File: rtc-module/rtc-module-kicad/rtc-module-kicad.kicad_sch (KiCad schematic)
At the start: 11 parts, among them J1 Battery-holder, J2 Microcontroller, U1 PCF8563T, Y1 Crystal - 32.768kHz

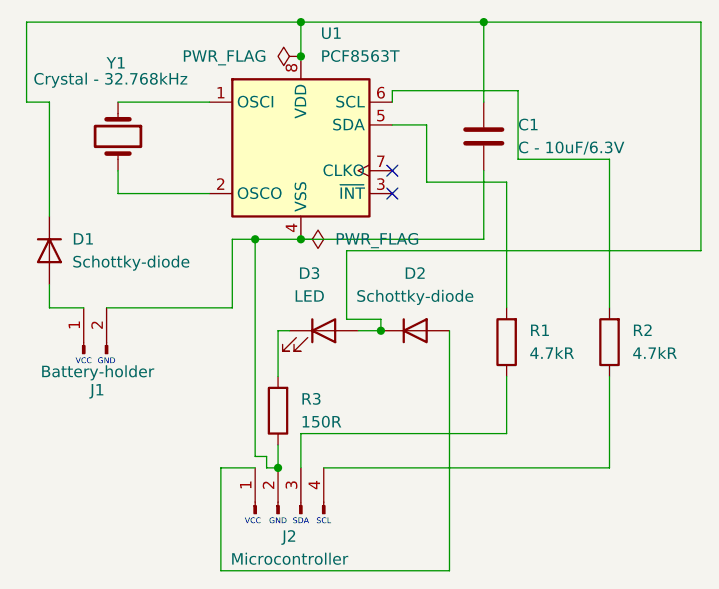
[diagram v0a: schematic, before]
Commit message: Connected items on the pcb.
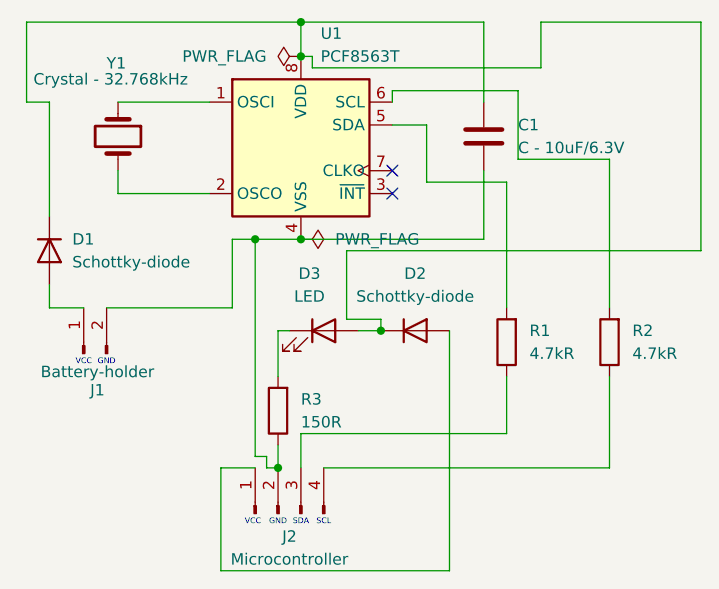
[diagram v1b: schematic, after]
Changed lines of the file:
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@@
 	(paper "A4")
-	(junction
-		(at 158.75 85.09)
-		(diameter 0)
-		(color 255 0 0 1)
-	)
 	(junction
 		(at 135.89 134.62)
@@
 	(wire
 		(pts
+			(xy 165.1 90.17) (xy 139.7 90.17)
+		)
+		(stroke
+			(width 0)
+			(type default)
+			(color 255 0 0 1)
+		)
+	)
+	(wire
+		(pts
 			(xy 162.56 100.33) (xy 162.56 92.71)
 		)
@@
 	(wire
 		(pts
+			(xy 139.7 90.17) (xy 139.7 88.9)
+		)
+		(stroke
+			(width 0)
+			(type default)
+			(color 255 0 0 1)
+		)
+	)
+	(wire
+		(pts
 			(xy 158.75 85.09) (xy 138.43 85.09)
 		)
@@
 	(wire
 		(pts
+			(xy 165.1 85.09) (xy 165.1 90.17)
+		)
+		(stroke
+			(width 0)
+			(type default)
+			(color 255 0 0 1)
+		)
+	)
+	(wire
+		(pts
 			(xy 107.95 93.98) (xy 107.95 85.09)
 		)
@@
 	(wire
 		(pts
+			(xy 139.7 88.9) (xy 138.43 88.9)
+		)
+		(stroke
+			(width 0)
+			(type default)
+			(color 255 0 0 1)
+		)
+	)
+	(wire
+		(pts
 			(xy 154.94 146.05) (xy 129.54 146.05)
 		)
@@
 	(wire
 		(pts
-			(xy 158.75 85.09) (xy 182.88 85.09)
-		)
-		(stroke
-			(width 0)
-			(type default)
-			(color 255 0 0 1)
-		)
-	)
-	(wire
-		(pts
 			(xy 118.11 104.14) (xy 128.27 104.14)
 		)
@@
 		)
 		(stroke
+			(width 0)
+			(type default)
+			(color 255 0 0 1)
+		)
+	)
+	(wire
+		(pts
+			(xy 182.88 85.09) (xy 165.1 85.09)
+		)
+		(stroke
